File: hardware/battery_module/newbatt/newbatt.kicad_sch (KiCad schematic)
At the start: 17 parts, among them J1 Barrel_Jack_MountingPin, J2 USB_C_Receptacle_PowerOnly_24P, J3 USB_B_Micro, J4 Screw_Terminal_01x02, J5 Screw_Terminal_01x02, U1 BQ25172DSGR

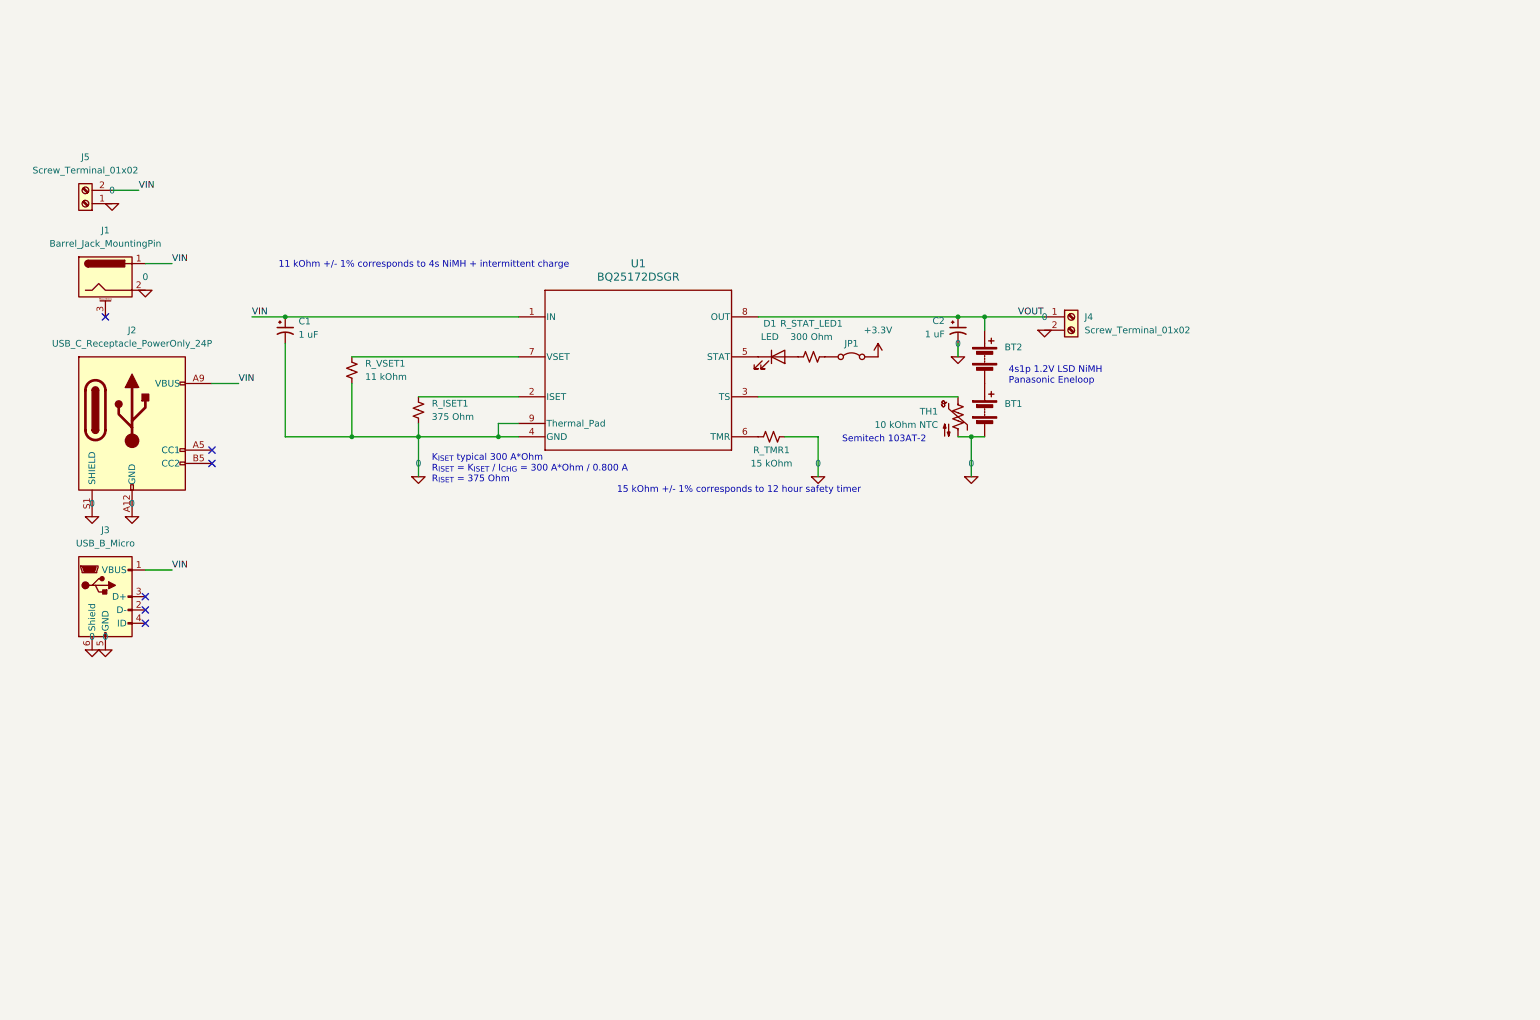
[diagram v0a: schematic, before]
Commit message: BQ25756E NiMH solar charging
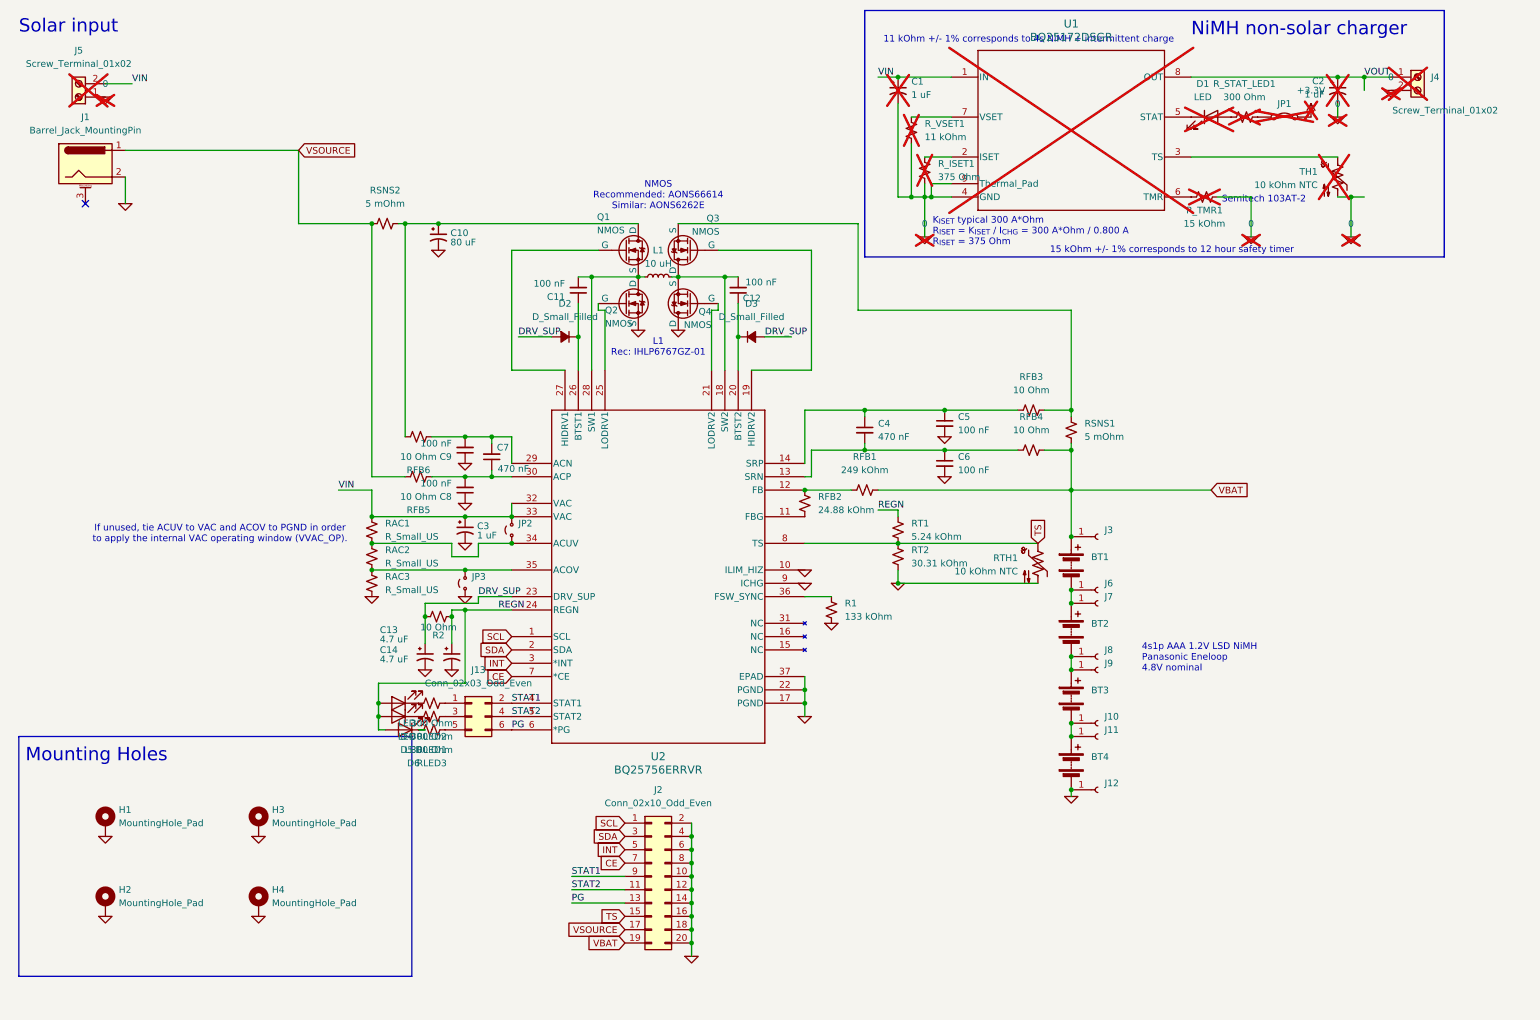
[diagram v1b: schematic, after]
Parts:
- removed J2: USB_C_Receptacle_PowerOnly_24P, Connector_USB:USB_C_Receptacle_CNCTech_C-ARA1-AK51X, symbol Connector:USB_C_Receptacle_PowerOnly_24P
- removed J3: USB_B_Micro, Connector_USB:USB_Micro-B_Amphenol_10118194_Horizontal, symbol Connector:USB_B_Micro
- added BT3, BT4: ~, Battery:BatteryHolder_Keystone_2468_2xAAA, symbol Device:Battery
- added C10: 80 uF, Capacitor_SMD:CP_Elec_10x10, symbol Device:C_Polarized_Small_US
- added C11, C12, C5, C6, C8, C9: 100 nF, Capacitor_SMD:C_0603_1608Metric, symbol Device:C_Small
- added C13, C14: 4.7 uF, Capacitor_SMD:CP_Elec_8x5.4, symbol Device:C_Polarized_Small_US
- added C3: 1 uF, Capacitor_SMD:CP_Elec_5x3, symbol Device:C_Polarized_Small_US
- added C4, C7: 470 nF, Capacitor_SMD:C_0603_1608Metric, symbol Device:C_Small
- added D2, D3: D_Small_Filled, Diode_SMD:D_0603_1608Metric, symbol Device:D_Small_Filled
- added D4, D5, D6: LED, LED_SMD:LED_0603_1608Metric, symbol Device:LED
- added H1, H2, H3, H4: MountingHole_Pad, MountingHole:MountingHole_3.2mm_M3_ISO7380_Pad_TopBottom, symbol Mechanical:MountingHole_Pad
- added J10, J11, J12, J3, J6, J7, J8, J9: Conn_01x01_Socket, Keystone82:BAT_82, symbol Connector:Conn_01x01_Socket
- added J13: Conn_02x03_Odd_Even, Connector_PinHeader_2.54mm:PinHeader_2x03_P2.54mm_Vertical, symbol Connector_Generic:Conn_02x03_Odd_Even
- added J2: Conn_02x10_Odd_Even, Connector_PinHeader_2.54mm:PinHeader_2x10_P2.54mm_Vertical, symbol Connector_Generic:Conn_02x10_Odd_Even
- added JP2, JP3: Jumper_2_Small_Open, Connector_PinHeader_2.54mm:PinHeader_1x02_P2.54mm_Vertical, symbol Jumper:Jumper_2_Small_Open
- added L1: 10 uH, Inductor_SMD:L_12x12mm_H8mm, symbol Device:L_Small
- added Q1, Q2, Q3, Q4: NMOS, Package_SON:VSONP-8-1EP_5x6_P1.27mm, symbol Simulation_SPICE:NMOS
- added R1: 133 kOhm, Resistor_SMD:R_0603_1608Metric, symbol Device:R_Small_US
- added R2, RFB3, RFB4, RFB5, RFB6: 10 Ohm, Resistor_SMD:R_0603_1608Metric, symbol Device:R_Small_US
- added RAC1, RAC2, RAC3: R_Small_US, Resistor_SMD:R_0603_1608Metric, symbol Device:R_Small_US
- added RFB1: 249 kOhm, Resistor_SMD:R_0603_1608Metric, symbol Device:R_Small_US
- added RFB2: 24.88 kOhm, Resistor_SMD:R_0603_1608Metric, symbol Device:R_Small_US
- added RLED1, RLED2, RLED3: 300 Ohm, Resistor_SMD:R_0603_1608Metric, symbol Device:R_Small_US
- added RSNS1, RSNS2: 5 mOhm, Resistor_SMD:R_0603_1608Metric, symbol Device:R_Small_US
- added RT1: 5.24 kOhm, Resistor_SMD:R_0603_1608Metric, symbol Device:R_Small_US
- added RT2: 30.31 kOhm, Resistor_SMD:R_0603_1608Metric, symbol Device:R_Small_US
- added RTH1: 10 kOhm NTC, Connector_PinHeader_2.54mm:PinHeader_1x02_P2.54mm_Vertical, symbol Device:Thermistor_NTC_US
- added U2: BQ25756ERRVR, BQ25756E:VQFN36_RRV_TEX, symbol BQ25756E:BQ25756ERRVR
- C1, C2: footprint Capacitor_THT:CP_Radial_D5.0mm_P2.50mm -> Capacitor_SMD:CP_Elec_5x3; now not fitted
- D1, J4, J5, JP1, TH1, U1: now not fitted
- J1: footprint Connector_BarrelJack:BarrelJack_Horizontal -> Connector_BarrelJack:BarrelJack_CUI_PJ-036AH-SMT_Horizontal
- R_ISET1, R_STAT_LED1, R_TMR1, R_VSET1: footprint Resistor_THT:R_Axial_DIN0309_L9.0mm_D3.2mm_P15.24mm_Horizontal -> Resistor_SMD:R_0603_1608Metric; now not fitted
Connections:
- net 0: now also BT4.2 (-), C10.2, C13.2, C14.2, C3.2, C5.2, C6.2, C8.1, C9.1, H1.1, H2.1, H3.1, H4.1, J12.1 (Pin_1), J2.10 (Pin_10), J2.12 (Pin_12), J2.14 (Pin_14), J2.16 (Pin_16), J2.18 (Pin_18), J2.2 (Pin_2), J2.20 (Pin_20), J2.4 (Pin_4), J2.6 (Pin_6), J2.8 (Pin_8), JP3.1 (A), Q2.3 (S), Q4.1 (D), R1.2, RAC3.2, RT2.2, RTH1.2, U2.10 (ILIM_HIZ), U2.17 (PGND), U2.22 (PGND), U2.37 (EPAD), U2.9 (ICHG); no longer BT1.2 (-)
- net VIN: now also C3.1, JP2.2 (B), RAC1.1, U2.32 (VAC), U2.33 (VAC); no longer J1.1
- net VOUT: no longer BT2.1 (+)
- net at BT2.2 (-): now also BT3.1 (+), J8.1 (Pin_1), J9.1 (Pin_1); no longer BT1.1 (+)
- new net: R1.1, U2.36 (FSW_SYNC)
- new net: JP3.2 (B), RAC2.2, RAC3.1, U2.35 (ACOV)
- new net: BT3.2 (-), BT4.1 (+), J10.1 (Pin_1), J11.1 (Pin_1)
- new net: C7.1, C8.2, RFB5.1, U2.30 (ACP)
- new net: Q3.3 (S), RFB3.2, RSNS1.1
- new net: C4.1, C5.1, RFB3.1, U2.14 (SRP)
- new net: C4.2, C6.1, RFB4.1, U2.13 (SRN)
- new net: BT1.2 (-), BT2.1 (+), J6.1 (Pin_1), J7.1 (Pin_1)
- new net: J13.5 (Pin_5), RLED3.1
- new net: D6.1 (K), RLED3.2
- new net: JP2.1 (A), RAC1.2, RAC2.1, U2.34 (ACUV)
- new net: J13.3 (Pin_3), RLED1.1
- new net: D5.1 (K), RLED1.2
- new net: C12.2, L1.2, Q3.1 (D), Q4.3 (S), U2.18 (SW2)
- new net: Q3.2 (G), U2.19 (HIDRV2)
- new net: C10.1, Q1.1 (D), RFB6.2, RSNS2.1
- new net: Q1.2 (G), U2.27 (HIDRV1)
- new net: C11.2, L1.1, Q1.3 (S), Q2.1 (D), U2.28 (SW1)
- new net: J13.1 (Pin_1), RLED2.1
- new net: C7.2, C9.2, RFB6.1, U2.29 (ACN)
- new net: D4.1 (K), RLED2.2
- new net: C12.1, D3.1 (K), U2.20 (BTST2)
- new net: RFB1.1, RFB2.1, U2.12 (FB)
- new net: Q2.2 (G), U2.25 (LODRV1)
- new net: C11.1, D2.1 (K), U2.26 (BTST1)
- new net: RFB2.2, U2.11 (FBG)
- new net: Q4.2 (G), U2.21 (LODRV2)
- new net CE: J2.7 (Pin_7), U2.7 (*CE)
- new net DRV_SUP: C13.1, D2.2 (A), D3.2 (A), R2.2, U2.23 (DRV_SUP)
- new net INT: J2.5 (Pin_5), U2.3 (*INT)
- new net PG: J13.6 (Pin_6), J2.13 (Pin_13), U2.6 (*PG)
- new net REGN: C14.1, D4.2 (A), D5.2 (A), D6.2 (A), R2.1, RT1.1, U2.24 (REGN)
- new net SCL: J2.1 (Pin_1), U2.1 (SCL)
- new net SDA: J2.3 (Pin_3), U2.2 (SDA)
- new net STAT1: J13.2 (Pin_2), J2.9 (Pin_9), U2.4 (STAT1)
- new net STAT2: J13.4 (Pin_4), J2.11 (Pin_11), U2.5 (STAT2)
- new net TS: J2.15 (Pin_15), RT1.2, RT2.1, RTH1.1, U2.8 (TS)
- new net VBAT: BT1.1 (+), J2.19 (Pin_19), J3.1 (Pin_1), RFB1.2, RFB4.2, RSNS1.2
- new net VSOURCE: J1.1, J2.17 (Pin_17), RFB5.2, RSNS2.2
- no-connect marks 6 -> 1
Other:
- note added: "4s1p AAA 1.2V LSD NiMH Panasonic Eneloop 4.8V nominal"
- note added: "If unused, tie ACUV to VAC and ACOV to PGND in order to apply the internal VAC operating window (VVAC_OP)."
- note added: "L1 Rec: IHLP6767GZ-01"
- note added: "Mounting Holes"
- note added: "NMOS Recommended: AONS66614 Similar: AONS6262E"
- note added: "NiMH non-solar charger"
- note added: "Solar input"
- note removed: "4s1p 1.2V LSD NiMH Panasonic Eneloop"
- moved on the sheet: BT1, J1

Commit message: 18650 Li-Ion 2 parallel design using BQ24210
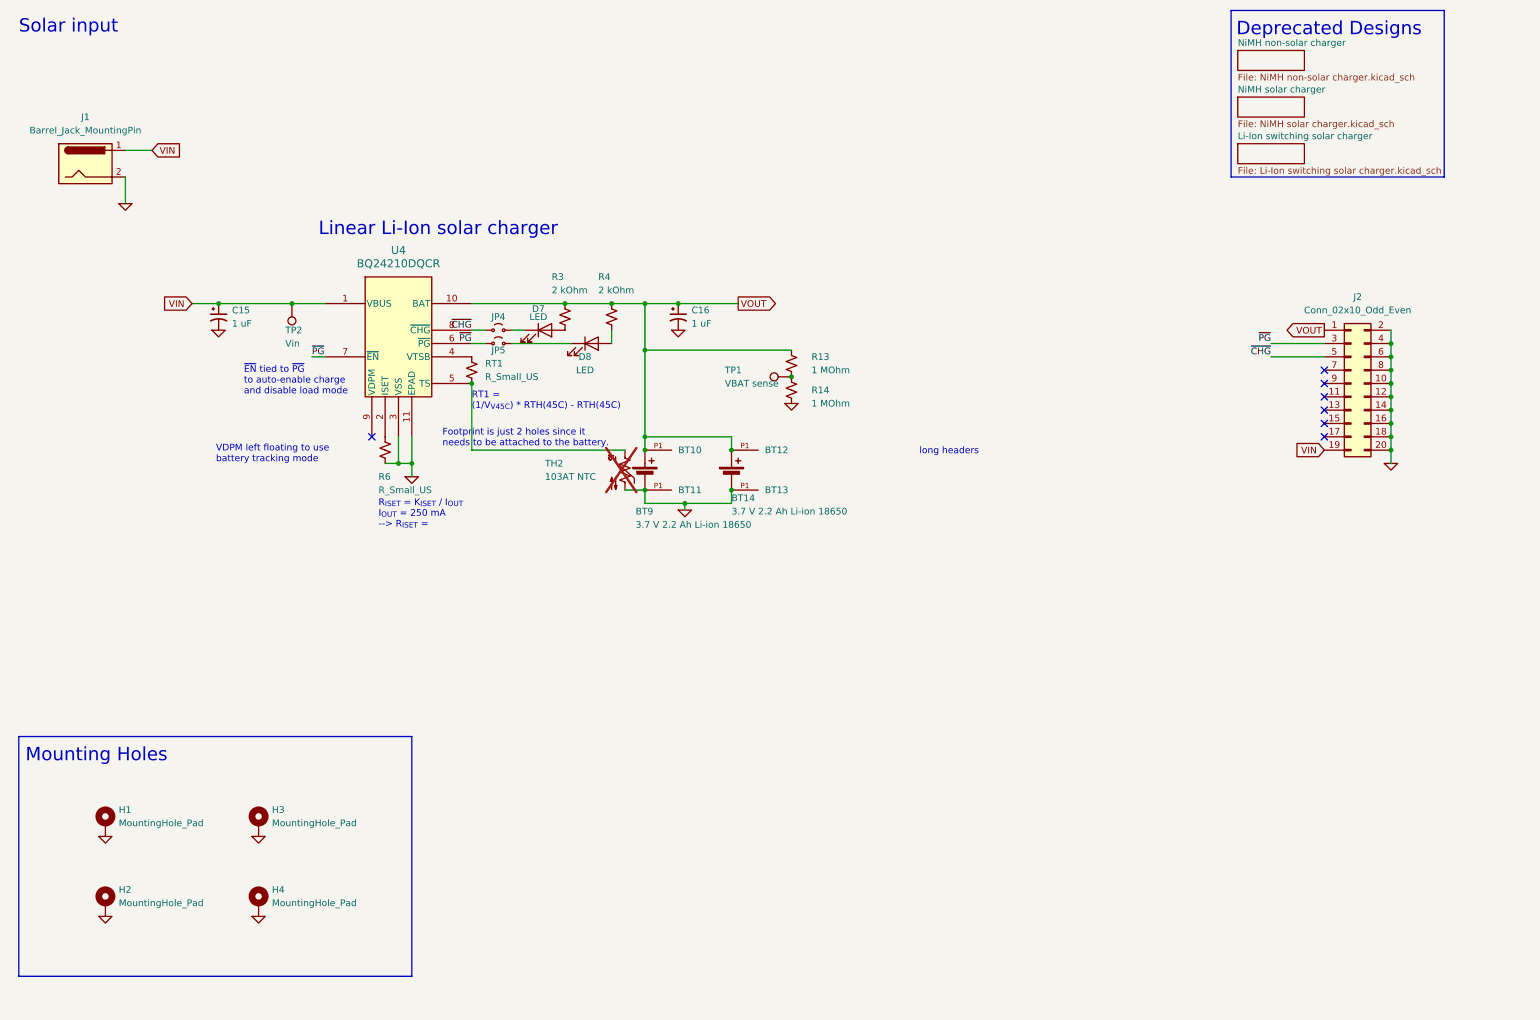
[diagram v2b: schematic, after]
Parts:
- removed BT1, BT2, BT3, BT4: ~, Battery:BatteryHolder_Keystone_2468_2xAAA, symbol Device:Battery
- removed C1, C2, C3: 1 uF, Capacitor_SMD:CP_Elec_5x3, symbol Device:C_Polarized_Small_US
- removed C10: 80 uF, Capacitor_SMD:CP_Elec_10x10, symbol Device:C_Polarized_Small_US
- removed C11, C12, C5, C6, C8, C9: 100 nF, Capacitor_SMD:C_0603_1608Metric, symbol Device:C_Small
- removed C13, C14: 4.7 uF, Capacitor_SMD:CP_Elec_8x5.4, symbol Device:C_Polarized_Small_US
- removed C4, C7: 470 nF, Capacitor_SMD:C_0603_1608Metric, symbol Device:C_Small
- removed D1, D4, D5, D6: LED, LED_SMD:LED_0603_1608Metric, symbol Device:LED
- removed D2, D3: D_Small_Filled, Diode_SMD:D_0603_1608Metric, symbol Device:D_Small_Filled
- removed J10, J11, J12, J3, J6, J7, J8, J9: Conn_01x01_Socket, Keystone82:BAT_82, symbol Connector:Conn_01x01_Socket
- removed J13: Conn_02x03_Odd_Even, Connector_PinHeader_2.54mm:PinHeader_2x03_P2.54mm_Vertical, symbol Connector_Generic:Conn_02x03_Odd_Even
- removed J4, J5: Screw_Terminal_01x02, TerminalBlock_Phoenix:TerminalBlock_Phoenix_MKDS-1,5-2-5.08_1x02_P5.08mm_Horizontal, symbol Connector:Screw_Terminal_01x02
- removed JP1: Jumper_2_Bridged, Connector_PinHeader_2.54mm:PinHeader_1x02_P2.54mm_Vertical, symbol Jumper:Jumper_2_Bridged
- removed JP2, JP3: Jumper_2_Small_Open, Connector_PinHeader_2.54mm:PinHeader_1x02_P2.54mm_Vertical, symbol Jumper:Jumper_2_Small_Open
- removed L1: 10 uH, Inductor_SMD:L_12x12mm_H8mm, symbol Device:L_Small
- removed Q1, Q2, Q3, Q4: NMOS, Package_SON:VSONP-8-1EP_5x6_P1.27mm, symbol Simulation_SPICE:NMOS
- removed R1: 133 kOhm, Resistor_SMD:R_0603_1608Metric, symbol Device:R_Small_US
- removed R2, RFB3, RFB4, RFB5, RFB6: 10 Ohm, Resistor_SMD:R_0603_1608Metric, symbol Device:R_Small_US
- removed RAC1, RAC2, RAC3: R_Small_US, Resistor_SMD:R_0603_1608Metric, symbol Device:R_Small_US
- removed RFB1: 249 kOhm, Resistor_SMD:R_0603_1608Metric, symbol Device:R_Small_US
- removed RFB2: 24.88 kOhm, Resistor_SMD:R_0603_1608Metric, symbol Device:R_Small_US
- removed RLED1, RLED2, RLED3, R_STAT_LED1: 300 Ohm, Resistor_SMD:R_0603_1608Metric, symbol Device:R_Small_US
- removed RSNS1, RSNS2: 5 mOhm, Resistor_SMD:R_0603_1608Metric, symbol Device:R_Small_US
- removed RT2: 30.31 kOhm, Resistor_SMD:R_0603_1608Metric, symbol Device:R_Small_US
- removed RTH1, TH1: 10 kOhm NTC, Connector_PinHeader_2.54mm:PinHeader_1x02_P2.54mm_Vertical, symbol Device:Thermistor_NTC_US
- removed R_ISET1: 375 Ohm, Resistor_SMD:R_0603_1608Metric, symbol Device:R_Small_US
- removed R_TMR1: 15 kOhm, Resistor_SMD:R_0603_1608Metric, symbol Device:R_Small_US
- removed R_VSET1: 11 kOhm, Resistor_SMD:R_0603_1608Metric, symbol Device:R_Small_US
- removed U1: BQ25172DSGR, BQ25172:DSG0008A-IPC_A, symbol BQ25172:BQ25172DSGR
- removed U2: BQ25756ERRVR, BQ25756E:VQFN36_RRV_TEX, symbol BQ25756E:BQ25756ERRVR
- added BT10, BT11, BT12, BT13: 254TR, Keystone254TR:BAT_254TR, symbol Keystone254TR:254TR
- added BT14, BT9: 3.7 V 2.2 Ah Li-ion 18650, Connector_JST:JST_PH_S2B-PH-K_1x02_P2.00mm_Horizontal, symbol Device:Battery_Cell
- added C15, C16: 1 uF, Capacitor_SMD:C_0603_1608Metric, symbol Device:C_Polarized_Small_US
- added D7, D8: LED, LED_SMD:LED_0603_1608Metric, symbol Device:LED
- added JP4, JP5: Jumper_2_Small_Open, Jumper:SolderJumper-2_P1.3mm_Open_RoundedPad1.0x1.5mm, symbol Jumper:Jumper_2_Small_Open
- added R13, R14: 1 MOhm, Resistor_SMD:R_0603_1608Metric, symbol Device:R_Small_US
- added R3, R4: 2 kOhm, Resistor_SMD:R_0603_1608Metric, symbol Device:R_Small_US
- added R6: R_Small_US, Resistor_SMD:R_0603_1608Metric, symbol Device:R_Small_US
- added TH2: 103AT NTC, Connector_PinHeader_2.54mm:PinHeader_1x02_P2.54mm_Vertical, symbol Device:Thermistor_NTC_US
- added TP1: VBAT sense, TestPoint:TestPoint_Pad_D1.5mm, symbol Connector:TestPoint
- added TP2: Vin, TestPoint:TestPoint_Pad_D1.5mm, symbol Connector:TestPoint
- added U4: BQ24210DQCR, BQ24210:DQC10_P84X2P4, symbol BQ24210:BQ24210DQCR
- J1: footprint Connector_BarrelJack:BarrelJack_CUI_PJ-036AH-SMT_Horizontal -> Connector_BarrelJack:BarrelJack_Horizontal; symbol Connector:Barrel_Jack_MountingPin -> Connector:Barrel_Jack
- RT1: value 5.24 kOhm -> R_Small_US
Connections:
- net SCL is gone; now on net VOUT: J2.1 (Pin_1)
- net VBAT is gone; now on net VIN: J2.19 (Pin_19)
- net 0: now also BT11.P1, BT13.P1, BT14.2 (-), BT9.2 (-), C15.2, C16.2, R14.2, R6.2, TH2.2, U4.11 (EPAD), U4.3 (VSS)
- net VIN: now also J1.1, C15.1, TP2.1, U4.1 (VBUS)
- net VOUT: now also BT10.P1, BT12.P1, BT14.1 (+), BT9.1 (+), C16.1, R13.1, R3.1, R4.1, U4.10 (BAT)
- net CE: no longer names the net of J2.7 (Pin_7)
- net INT renamed ~{CHG}
- net ~{CHG}: now also JP4.1 (A), U4.8 (~{CHG})
- net PG: no longer names the net of J2.13 (Pin_13)
- net REGN: no longer names the net of RT1.1
- net REGN: now also U4.4 (VTSB)
- net SDA renamed ~{PG}
- net ~{PG}: now also JP5.1 (A), U4.6 (~{PG}), U4.7 (~{EN})
- net STAT1: no longer names the net of J2.9 (Pin_9)
- net STAT2: no longer names the net of J2.11 (Pin_11)
- net TS: no longer names the net of RT1.2
- net TS: now also TH2.1, U4.5 (TS); no longer J2.15 (Pin_15)
- net VSOURCE: no longer names the net of J2.17 (Pin_17)
- net VSOURCE: no longer J1.1
- new net: D7.1 (K), JP4.2 (B)
- new net: R13.2, R14.1, TP1.1
- new net: D7.2 (A), R3.2
- new net: D8.1 (K), JP5.2 (B)
- new net: D8.2 (A), R4.2
- new net: R6.1, U4.2 (ISET)
- no-connect marks 1 -> 7
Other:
- added sheet Li-Ion switching solar charger (Li-Ion switching solar charger.kicad_sch)
- added sheet NiMH non-solar charger (NiMH non-solar charger.kicad_sch)
- added sheet NiMH solar charger (NiMH solar charger.kicad_sch)
- note added: "Deprecated Designs"
- note added: "Footprint is just 2 holes since it needs to be attached to the battery."
- note added: "Linear Li-Ion solar charger"
- note added: "RT1 = (1/V_{V45C}) * RTH(45C) - RTH(45C)"
- note added: "R_{ISET} = K_{ISET} / I_{OUT} I_{OUT} = 250 mA --> R_{ISET} ="
- note added: "VDPM left floating to use battery tracking mode"
- note added: "long headers"
- note added: "~{EN} tied to ~{PG} to auto-enable charge and disable load mode"
- note removed: "11 kOhm +/- 1% corresponds to 4s NiMH + intermittent charge"
- note removed: "15 kOhm +/- 1% corresponds to 12 hour safety timer"
- note removed: "4s1p AAA 1.2V LSD NiMH Panasonic Eneloop 4.8V nominal"
- note removed: "If unused, tie ACUV to VAC and ACOV to PGND in order to apply the internal VAC operating window (VVAC_OP)."
- note removed: "K_{ISET} typical 300 A*Ohm R_{ISET} = K_{ISET} / I_{CHG} = 300 A*Ohm / 0.800 A R_{ISET} = 375 Ohm"
- note removed: "L1 Rec: IHLP6767GZ-01"
- note removed: "NMOS Recommended: AONS66614 Similar: AONS6262E"
- note removed: "NiMH non-solar charger"
- note removed: "Semitech 103AT-2"
- moved on the sheet: J2
